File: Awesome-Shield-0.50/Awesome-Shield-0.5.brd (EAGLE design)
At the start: 51 x 55 mm, 37 parts, among them SW1 SPST_TACT-EVQQ2, SW2 DPDT, U1 LIGHTSENSORTEMT6000

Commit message: added refdes labels for THT parts to silkscreen, image export broken - images out of date
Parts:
- renumbered J3 to J1, J4 to J2
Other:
- board text added: "J1"
- board text added: "J2"
- board text added: "RV1"

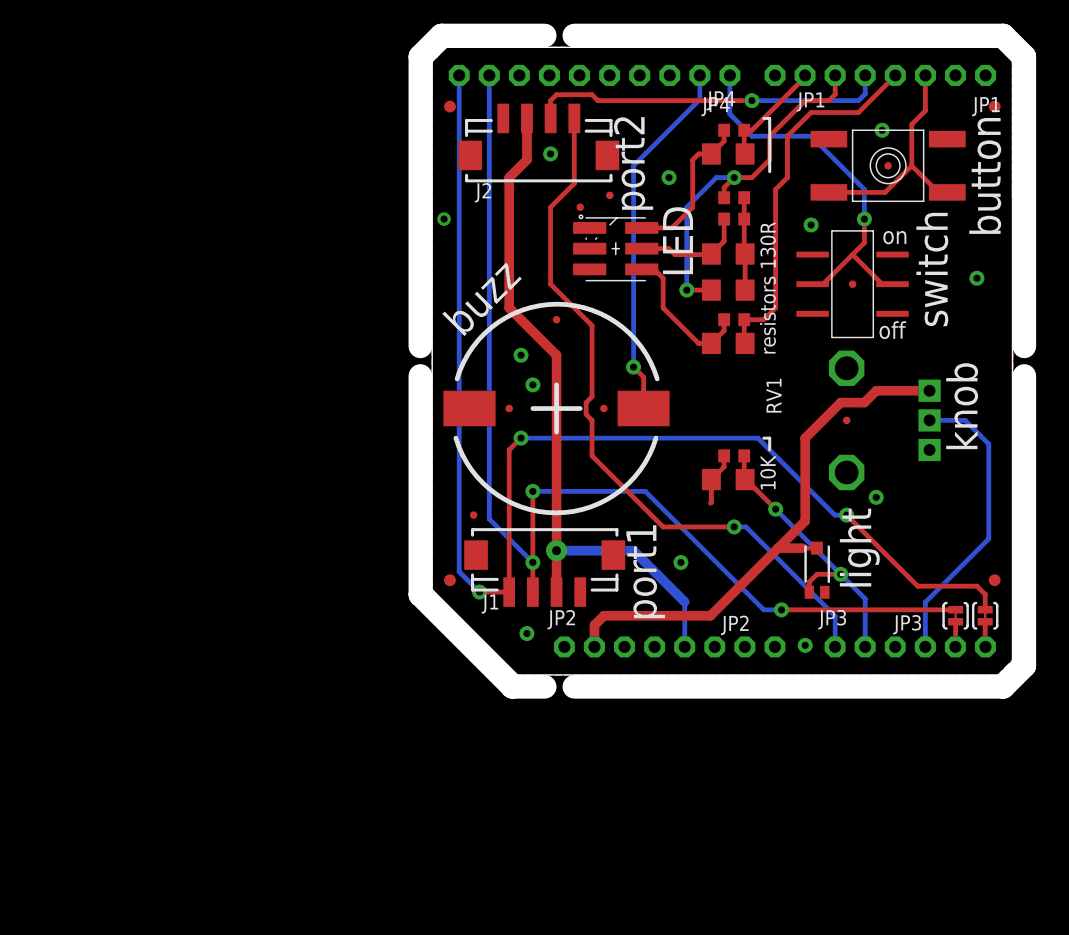
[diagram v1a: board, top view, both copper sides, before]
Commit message: reorganizing filetree for RFQ, added mounts and readme for RFQ
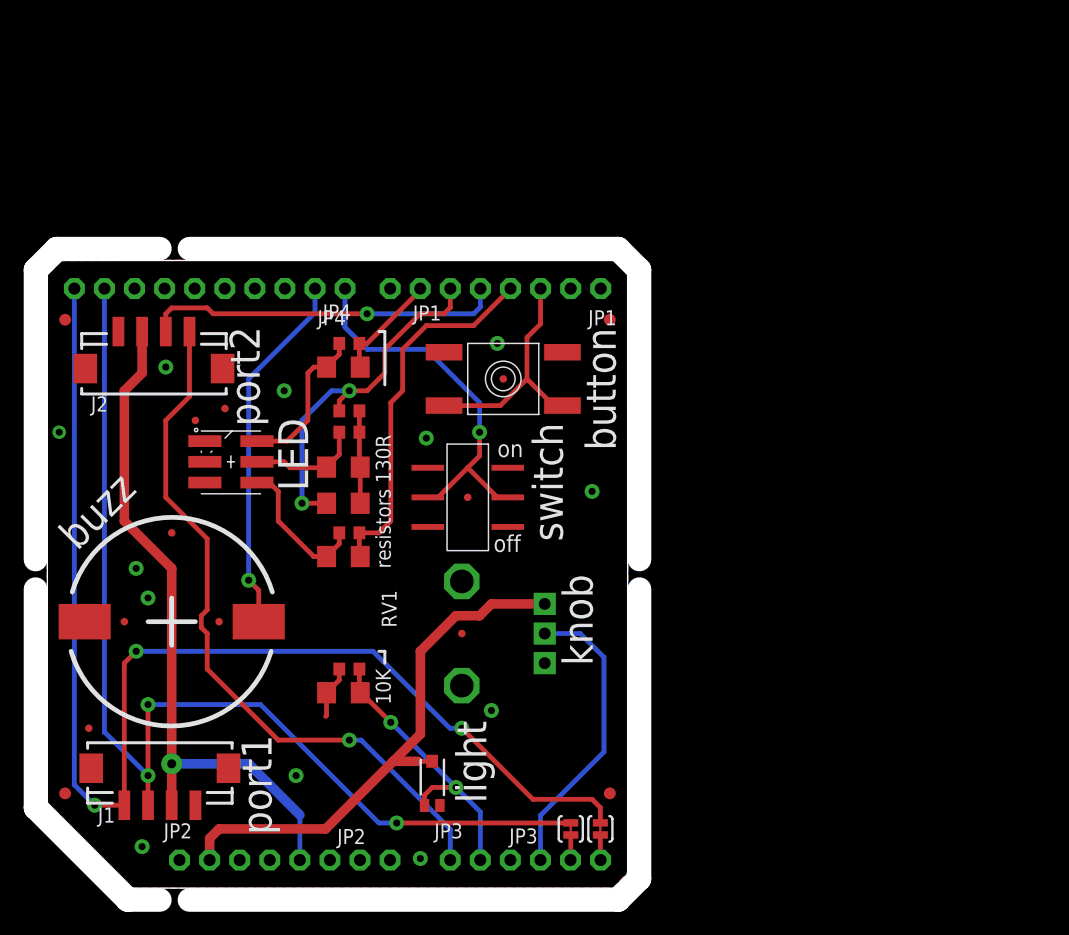
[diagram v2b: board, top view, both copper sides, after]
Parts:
- moved JP3 37.2 mm to (40.4, 2.37)
- moved FID1 37.2 mm to (1.50, 8.00)
- moved FID10 37.2 mm to (6.50, 22.5)
- moved FID11 37.2 mm to (35.0, 21.5)
- moved FID13 37.2 mm to (35.5, 33.0)
- moved FID15 37.2 mm to (15.0, 40.5)
- moved FID2 37.2 mm to (47.5, 48.0)
- moved FID3 37.2 mm to (47.5, 8.00)
- moved FID4 37.2 mm to (1.50, 48.0)
- moved FID5 37.2 mm to (3.50, 13.5)
- moved FID6 37.2 mm to (12.5, 39.5)
- moved FID7 37.2 mm to (38.5, 43.0)
- moved FID8 37.2 mm to (14.5, 22.5)
- moved FID9 37.2 mm to (10.5, 30.0)
- moved J1 37.2 mm to (9.50, 7.00)
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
